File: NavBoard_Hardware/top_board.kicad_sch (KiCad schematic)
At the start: 8 parts, among them J13 Conn_01x16, J14 Conn_01x16, J15 Conn_01x03, J16 Conn_01x03

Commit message: Created adapter symbols and footprints
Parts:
- removed J13, J14: Conn_01x16, symbol Connector_Generic:Conn_01x16
- added J? (x2): Conn_02x16_Separate, Nav_Board:PinSocket_2x16_P2.54mm_Vertical_Nav_Board, symbol Nav_Board:Conn_02x16_Separate
- gave numbers to parts that had none: 4
- renumbered J15 to J4, J16 to J6
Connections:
- net Pin10L: now also J?.10
- net Pin10R: now also J?.26
- net Pin11L: now also J?.11
- net Pin11R: now also J?.27
- net Pin12L: now also J?.12
- net Pin12R: now also J?.28
- net Pin13L: now also J?.13
- net Pin13R: now also J?.29
- net Pin14L: now also J?.14
- net Pin14R: now also J?.30
- net Pin15L: now also J?.15
- net Pin15R: now also J?.31
- net Pin16L: now also J?.16
- net Pin16R: now also J?.32
- net Pin1L: now also J?.1
- net Pin1R: now also J?.17
- net Pin2L: now also J?.2
- net Pin2R: now also J?.18
- net Pin3L: now also J?.3
- net Pin3R: now also J?.19
- net Pin4L: now also J?.4
- net Pin4R: now also J?.20
- net Pin5L: now also J?.5
- net Pin5R: now also J?.21
- net Pin6L: now also J?.6
- net Pin6R: now also J?.22
- net Pin7L: now also J?.7
- net Pin7R: now also J?.23
- net Pin8L: now also J?.8
- net Pin8R: now also J?.24
- net Pin9L: now also J?.9
- net Pin9R: now also J?.25

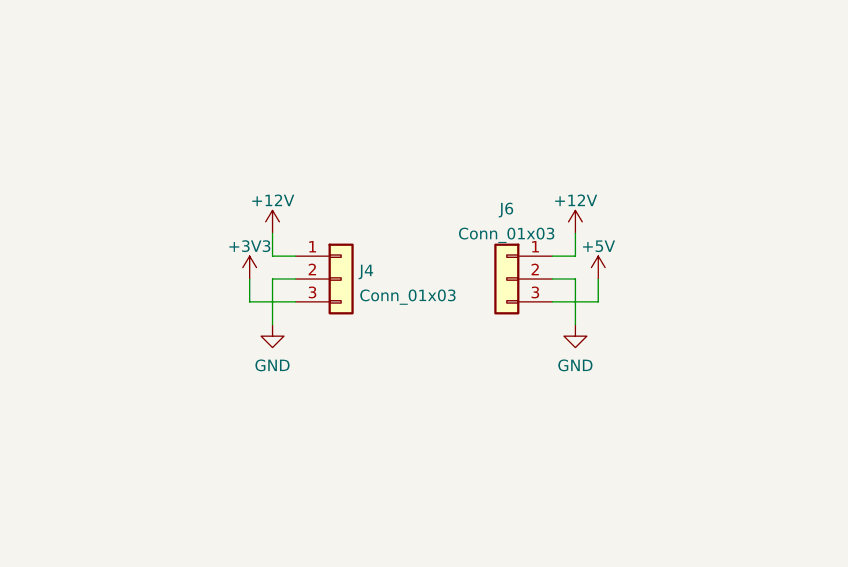
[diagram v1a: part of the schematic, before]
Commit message: Updated BMI component sheet from Navboard_2023_rev2
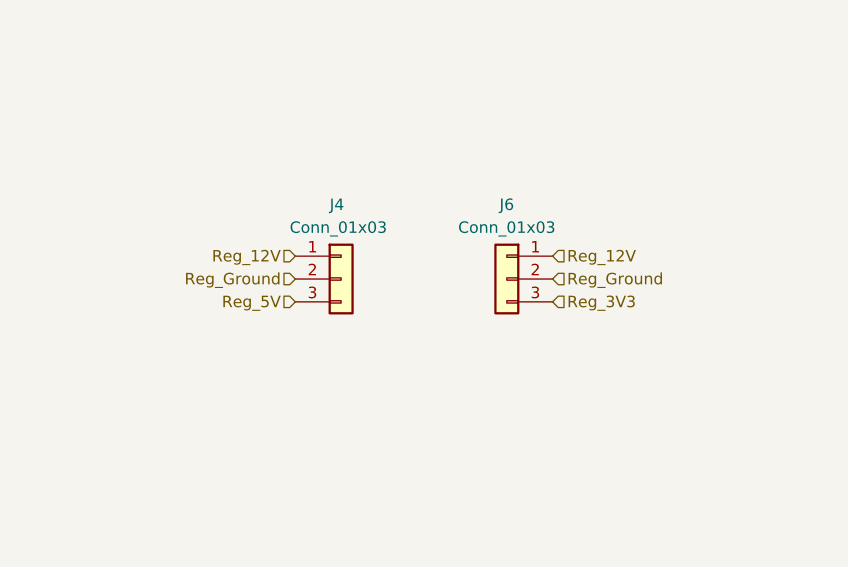
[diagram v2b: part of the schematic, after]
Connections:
- net +5V: no longer J6.3 (Pin_3)
- net GND: no longer J4.2 (Pin_2), J6.2 (Pin_2)
- net +12V renamed Reg_12V
- net +3V3 renamed Reg_5V
- new net Reg_3V3: J6.3 (Pin_3)
- new net Reg_Ground: J4.2 (Pin_2), J6.2 (Pin_2)
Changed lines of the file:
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@@
 (kicad_sch (version 20211123) (generator eeschema)
   (paper "A4")
-  (wire (pts (xy 194.31 84.455) (xy 189.23 84.455))
-    (stroke (width 0) (type default) (color 0 0 0 0))
-  )
   (wire (pts (xy 139.065 168.91) (xy 139.065 170.18))
     (stroke (width 0) (type default) (color 0 0 0 0))
@@
     (stroke (width 0) (type default) (color 0 0 0 0))
   )
-  (wire (pts (xy 155.575 81.915) (xy 155.575 84.455))
-    (stroke (width 0) (type default) (color 0 0 0 0))
-  )
   (wire (pts (xy 235.585 100.33) (xy 225.425 100.33))
     (stroke (width 0) (type default) (color 0 0 0 0))
@@
     (stroke (width 0) (type default) (color 0 0 0 0))
   )
-  (wire (pts (xy 191.77 86.995) (xy 191.77 81.915))
-    (stroke (width 0) (type default) (color 0 0 0 0))
-  )
   (wire (pts (xy 182.245 153.035) (xy 183.515 153.035))
     (stroke (width 0) (type default) (color 0 0 0 0))
@@
     (stroke (width 0) (type default) (color 0 0 0 0))
   )
-  (wire (pts (xy 158.115 76.835) (xy 158.115 79.375))
-    (stroke (width 0) (type default) (color 0 0 0 0))
-  )
   (wire (pts (xy 182.245 147.955) (xy 191.135 147.955))
     (stroke (width 0) (type default) (color 0 0 0 0))
   )
-  (wire (pts (xy 158.115 81.915) (xy 160.655 81.915))
-    (stroke (width 0) (type default) (color 0 0 0 0))
-  )
   (wire (pts (xy 180.975 160.02) (xy 183.515 160.02))
     (stroke (width 0) (type default) (color 0 0 0 0))
@@
     (stroke (width 0) (type default) (color 0 0 0 0))
   )
-  (wire (pts (xy 191.77 81.915) (xy 189.23 81.915))
-    (stroke (width 0) (type default) (color 0 0 0 0))
-  )
-  (wire (pts (xy 155.575 84.455) (xy 160.655 84.455))
-    (stroke (width 0) (type default) (color 0 0 0 0))
-  )
   (wire (pts (xy 235.585 105.41) (xy 225.425 105.41))
     (stroke (width 0) (type default) (color 0 0 0 0))
@@
     (stroke (width 0) (type default) (color 0 0 0 0))
   )
-  (wire (pts (xy 158.115 86.995) (xy 158.115 81.915))
-    (stroke (width 0) (type default) (color 0 0 0 0))
-  )
   (wire (pts (xy 183.515 153.035) (xy 183.515 160.02))
-    (stroke (width 0) (type default) (color 0 0 0 0))
-  )
-  (wire (pts (xy 191.77 76.835) (xy 191.77 79.375))
-    (stroke (width 0) (type default) (color 0 0 0 0))
-  )
-  (wire (pts (xy 191.77 79.375) (xy 189.23 79.375))
-    (stroke (width 0) (type default) (color 0 0 0 0))
-  )
-  (wire (pts (xy 158.115 79.375) (xy 160.655 79.375))
-    (stroke (width 0) (type default) (color 0 0 0 0))
-  )
-  (wire (pts (xy 194.31 81.915) (xy 194.31 84.455))
     (stroke (width 0) (type default) (color 0 0 0 0))
   )
@@
     (effects (font (size 1.27 1.27)) (justify left))
   )
+  (hierarchical_label "Reg_3V3" (shape input) (at 189.23 84.455 0)
+    (effects (font (size 1.27 1.27)) (justify left))
+  )
   (hierarchical_label "Pin5L" (shape input) (at 92.71 88.9 180)
     (effects (font (size 1.27 1.27)) (justify right))
@@
     (effects (font (size 1.27 1.27)) (justify left))
   )
+  (hierarchical_label "Reg_Ground" (shape input) (at 189.23 81.915 0)
+    (effects (font (size 1.27 1.27)) (justify left))
+  )
   (hierarchical_label "Pin3L" (shape input) (at 92.71 83.82 180)
     (effects (font (size 1.27 1.27)) (justify right))
@@
     (effects (font (size 1.27 1.27)) (justify left))
   )
+  (hierarchical_label "Reg_Ground" (shape input) (at 160.655 81.915 180)
+    (effects (font (size 1.27 1.27)) (justify right))
+  )
   (hierarchical_label "Pin5R" (shape input) (at 110.49 88.9 0)
     (effects (font (size 1.27 1.27)) (justify left))
@@
     (effects (font (size 1.27 1.27)) (justify left))
   )
+  (hierarchical_label "Reg_12V" (shape input) (at 160.655 79.375 180)
+    (effects (font (size 1.27 1.27)) (justify right))
+  )
   (hierarchical_label "Pin8R" (shape input) (at 110.49 96.52 0)
     (effects (font (size 1.27 1.27)) (justify left))
@@
     (effects (font (size 1.27 1.27)) (justify right))
   )
+  (hierarchical_label "Reg_12V" (shape input) (at 189.23 79.375 0)
+    (effects (font (size 1.27 1.27)) (justify left))
+  )
+  (hierarchical_label "Reg_5V" (shape input) (at 160.655 84.455 180)
+    (effects (font (size 1.27 1.27)) (justify right))
+  )
   (hierarchical_label "Pin4R" (shape input) (at 110.49 86.36 0)
     (effects (font (size 1.27 1.27)) (justify left))
@@
     (pin "2")
   )
-  (symbol (lib_id "power:GND") (at 191.77 86.995 0) (unit 1)
-    (in_bom yes) (on_board yes) (fields_autoplaced)
-    (property "Reference" "#PWR039" (id 0) (at 191.77 93.345 0)
-      (effects (font (size 1.27 1.27)) hide)
-    )
-    (property "Value" "GND" (id 1) (at 191.77 91.5575 0))
-    (property "Footprint" "" (id 2) (at 191.77 86.995 0)
-      (effects (font (size 1.27 1.27)) hide)
-    )
-    (property "Datasheet" "" (id 3) (at 191.77 86.995 0)
-      (effects (font (size 1.27 1.27)) hide)
-    )
-    (pin "1")
-  )
-  (symbol (lib_id "power:+12V") (at 158.115 76.835 0) (mirror y) (unit 1)
-    (in_bom yes) (on_board yes) (fields_autoplaced)
-    (property "Reference" "#PWR034" (id 0) (at 158.115 80.645 0)
-      (effects (font (size 1.27 1.27)) hide)
-    )
-    (property "Value" "+12V" (id 1) (at 158.115 73.2305 0))
-    (property "Footprint" "" (id 2) (at 158.115 76.835 0)
-      (effects (font (size 1.27 1.27)) hide)
-    )
-    (property "Datasheet" "" (id 3) (at 158.115 76.835 0)
-      (effects (font (size 1.27 1.27)) hide)
-    )
-    (pin "1")
-  )
   (symbol (lib_id "Connector_Generic:Conn_01x03") (at 165.735 81.915 0) (unit 1)
-    (in_bom yes) (on_board yes) (fields_autoplaced)
-    (property "Reference" "J4" (id 0) (at 167.767 81.0065 0)
-      (effects (font (size 1.27 1.27)) (justify left))
-    )
-    (property "Value" "Conn_01x03" (id 1) (at 167.767 83.7816 0)
+    (in_bom yes) (on_board yes)
+    (property "Reference" "J4" (id 0) (at 164.465 73.66 0)
+      (effects (font (size 1.27 1.27)) (justify left))
+    )
+    (property "Value" "Conn_01x03" (id 1) (at 160.02 76.2 0)
       (effects (font (size 1.27 1.27)) (justify left))
     )
@@
     (pin "2")
     (pin "3")
-  )
-  (symbol (lib_id "power:GND") (at 158.115 86.995 0) (mirror y) (unit 1)
-    (in_bom yes) (on_board yes) (fields_autoplaced)
-    (property "Reference" "#PWR035" (id 0) (at 158.115 93.345 0)
-      (effects (font (size 1.27 1.27)) hide)
-    )
-    (property "Value" "GND" (id 1) (at 158.115 91.5575 0))
-    (property "Footprint" "" (id 2) (at 158.115 86.995 0)
-      (effects (font (size 1.27 1.27)) hide)
-    )
-    (property "Datasheet" "" (id 3) (at 158.115 86.995 0)
-      (effects (font (size 1.27 1.27)) hide)
-    )
-    (pin "1")
   )
   (symbol (lib_id "Device:R_US") (at 134.62 165.1 0) (unit 1)
@@
     (pin "1")
   )
-  (symbol (lib_id "power:+12V") (at 191.77 76.835 0) (unit 1)
-    (in_bom yes) (on_board yes) (fields_autoplaced)
-    (property "Reference" "#PWR038" (id 0) (at 191.77 80.645 0)
-      (effects (font (size 1.27 1.27)) hide)
-    )
-    (property "Value" "+12V" (id 1) (at 191.77 73.2305 0))
-    (property "Footprint" "" (id 2) (at 191.77 76.835 0)
-      (effects (font (size 1.27 1.27)) hide)
-    )
-    (property "Datasheet" "" (id 3) (at 191.77 76.835 0)
-      (effects (font (size 1.27 1.27)) hide)
-    )
-    (pin "1")
-  )
   (symbol (lib_id "Connector_Generic:Conn_01x03") (at 184.15 81.915 0) (mirror y) (unit 1)
-    (in_bom yes) (on_board yes) (fields_autoplaced)
-    (property "Reference" "J6" (id 0) (at 184.15 74.1385 0))
-    (property "Value" "Conn_01x03" (id 1) (at 184.15 76.9136 0))
+    (in_bom yes) (on_board yes)
+    (property "Reference" "J6" (id 0) (at 184.15 73.66 0))
+    (property "Value" "Conn_01x03" (id 1) (at 184.15 76.2 0))
     (property "Footprint" "" (id 2) (at 184.15 81.915 0)
       (effects (font (size 1.27 1.27)) hide)
@@
     (pin "6")
   )
-  (symbol (lib_id "power:+5V") (at 194.31 81.915 0) (unit 1)
-    (in_bom yes) (on_board yes) (fields_autoplaced)
-    (property "Reference" "#PWR040" (id 0) (at 194.31 85.725 0)
-      (effects (font (size 1.27 1.27)) hide)
-    )
-    (property "Value" "+5V" (id 1) (at 194.31 78.3105 0))
-    (property "Footprint" "" (id 2) (at 194.31 81.915 0)
-      (effects (font (size 1.27 1.27)) hide)
-    )
-    (property "Datasheet" "" (id 3) (at 194.31 81.915 0)
-      (effects (font (size 1.27 1.27)) hide)
-    )
-    (pin "1")
-  )
   (symbol (lib_id "power:GND") (at 258.445 50.8 0) (unit 1)
     (in_bom yes) (on_board yes)
@@
       (effects (font (size 1.27 1.27)) hide)
     )
-    (pin "1")
-  )
-  (symbol (lib_id "power:+3V3") (at 155.575 81.915 0) (unit 1)
-    (in_bom yes) (on_board yes) (fields_autoplaced)
-    (property "Reference" "#PWR033" (id 0) (at 155.575 85.725 0)
-      (effects (font (size 1.27 1.27)) hide)
-    )
-    (property "Value" "+3V3" (id 1) (at 155.575 78.3105 0))
-    (property "Footprint" "" (id 2) (at 155.575 81.915 0)
-      (effects (font (size 1.27 1.27)) hide)
-    )
-    (property "Datasheet" "" (id 3) (at 155.575 81.915 0)
-      (effects (font (size 1.27 1.27)) hide)
-    )

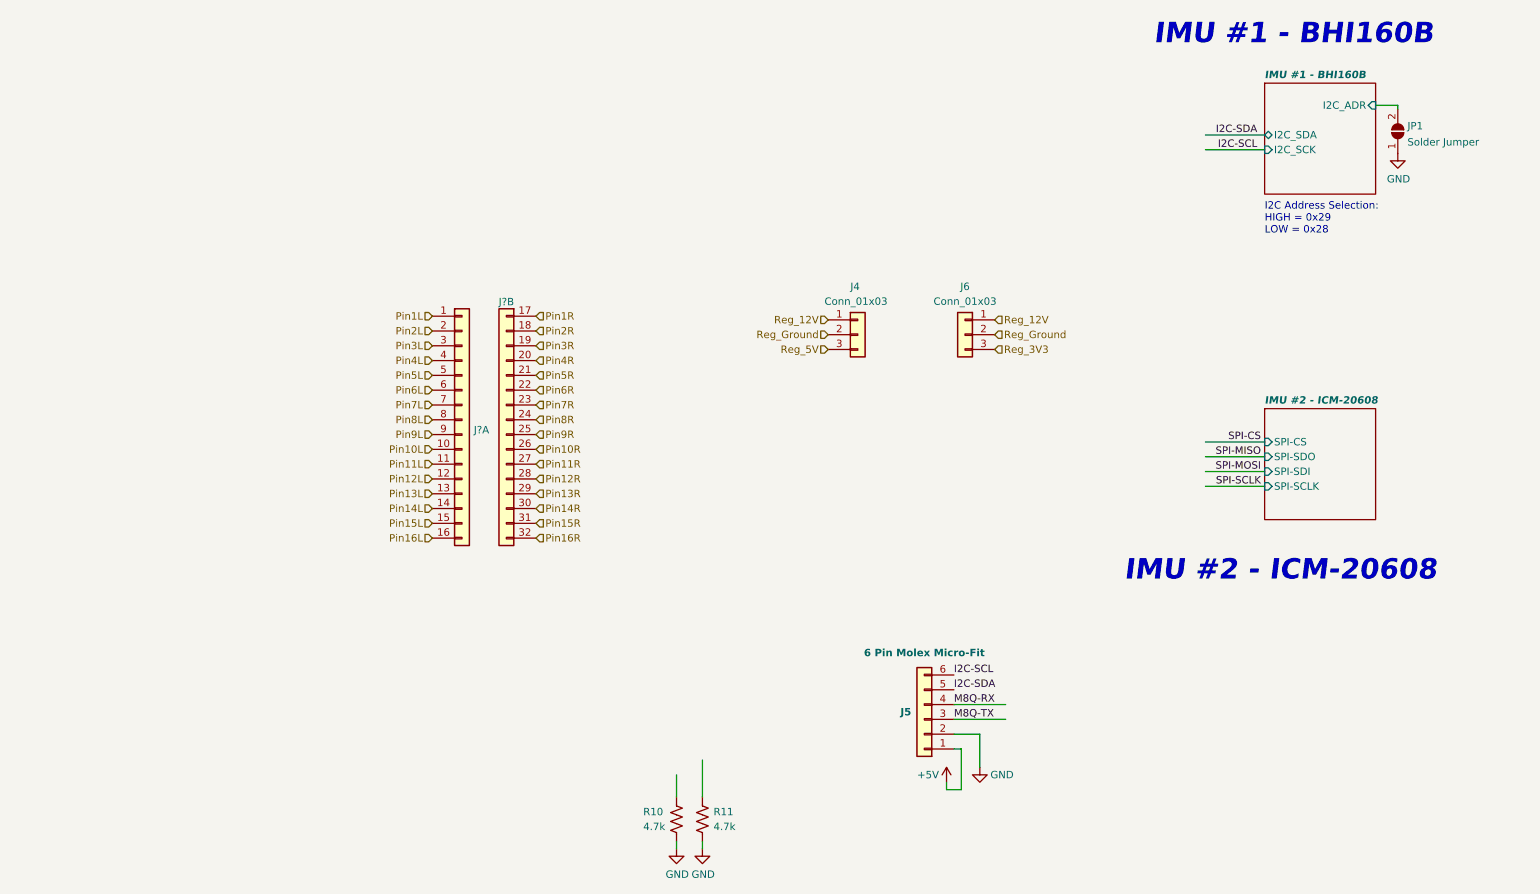
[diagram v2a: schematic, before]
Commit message: Most schematic connections completed
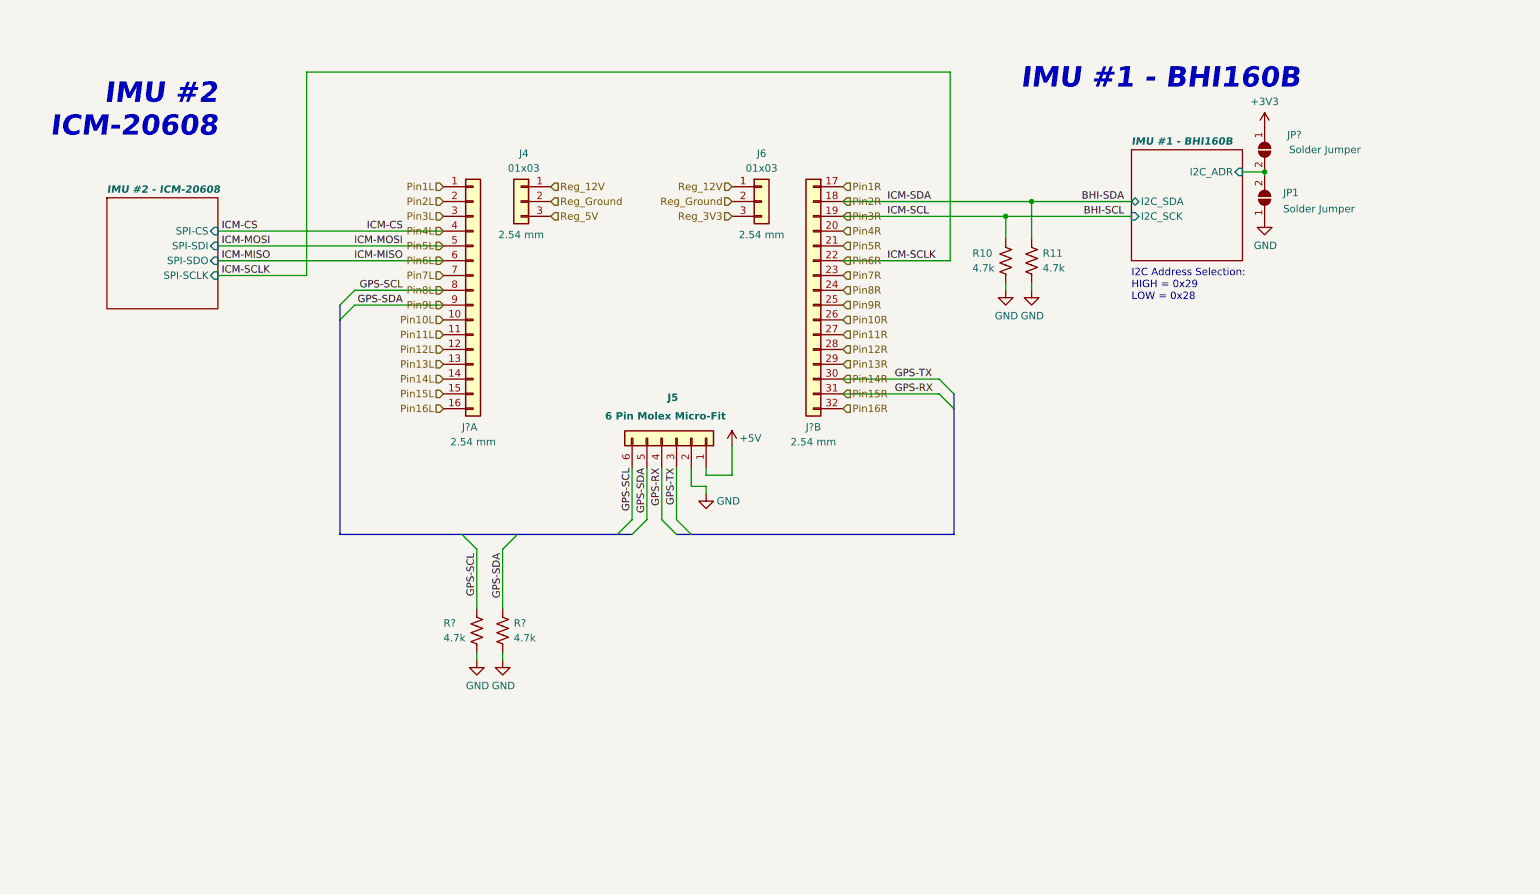
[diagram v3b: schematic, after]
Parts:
- added JP?: Solder Jumper, Jumper:SolderJumper-2_P1.3mm_Open_RoundedPad1.0x1.5mm, symbol Jumper:SolderJumper_2_Open
- added R? (x2): 4.7k, Resistor_SMD:R_0603_1608Metric_Pad0.98x0.95mm_HandSolder, symbol Device:R_US
- J4, J6: value Conn_01x03 -> 01x03; Field4 (none) -> 2.54 mm
- J? (x2): Field4 (none) -> 2.54 mm
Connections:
- net I2C-SCL is gone; now on net Pin8L: J5.6 (Pin_6)
- net I2C-SDA is gone; now on net Pin9L: J5.5 (Pin_5)
- net M8Q-RX is gone; now on net Pin15R: J5.4 (Pin_4)
- net M8Q-TX is gone; now on net Pin14R: J5.3 (Pin_3)
- net GND: now also R?.2, R?.2
- net IMU #1 - BHI160B/I2C_ADR: now also JP?.2 (B)
- net Pin2R: now also R11.1
- net Pin3R: now also R10.1
- net Pin8L: now also R?.1
- net Pin9L: now also R?.1
- new net +3V3: JP?.1 (A)
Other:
- note added: "IMU #2 ICM-20608"
- note removed: "IMU #2 - ICM-20608"
- moved on the sheet: J4, J5, J6, J?A, J?B, JP1, R10, R11
